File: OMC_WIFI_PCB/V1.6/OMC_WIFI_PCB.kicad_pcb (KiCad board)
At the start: 2 copper layers, 106.8 x 66.8 mm, 26 parts, among them J1 Conn_01x02_Male, J10 Conn_01x01_Male, J2 Conn_01x02_Female, J3 Conn_01x02_Male, J4 Switch, J5 Pins_FT232R, J6 Level shifter, J7 Conn_01x01_Female, J8 Regulador, J9 Conn_01x01_Female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

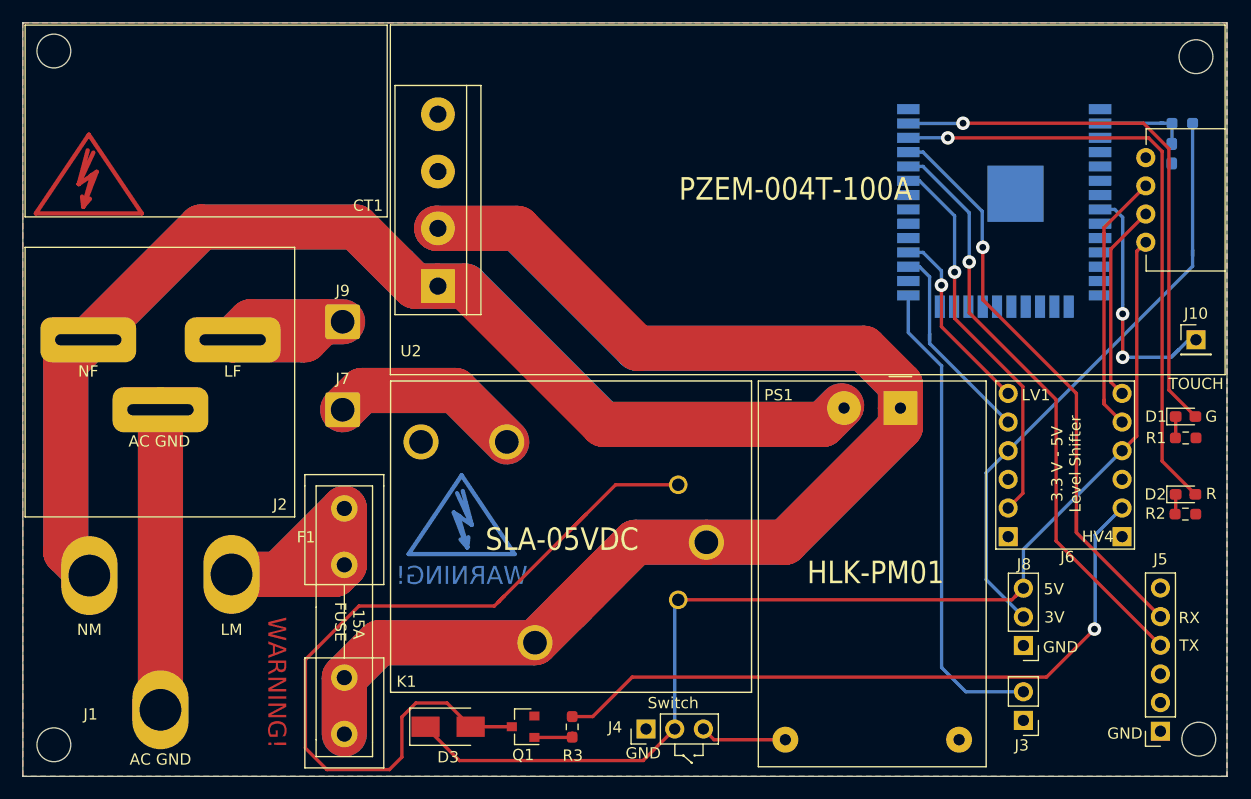
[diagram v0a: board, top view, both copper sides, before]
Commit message: Creación de versión 1.6 PCB
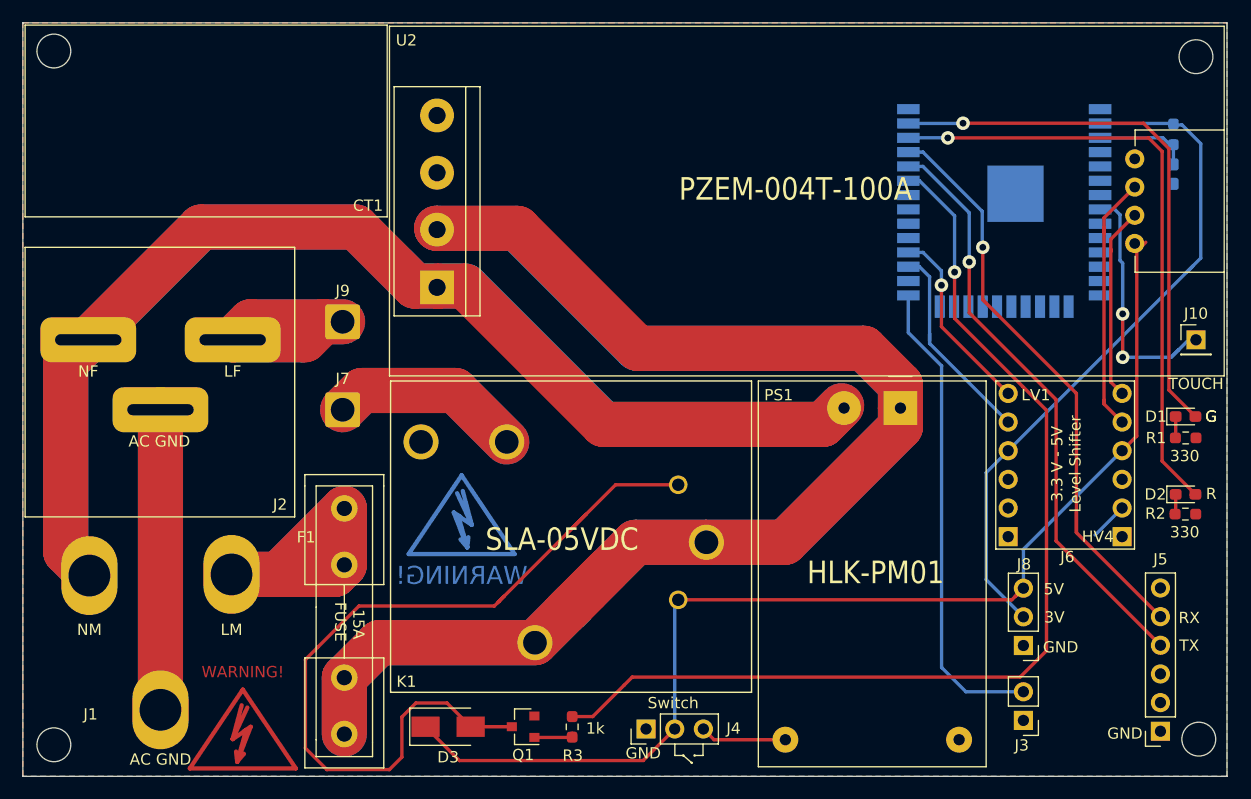
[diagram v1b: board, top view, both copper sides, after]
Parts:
- moved SYM1 51.1 mm to (595.5, -918.2)
- moved C1 1.82 mm to (678.0, -968.1)
- moved R4 1.26 mm to (678.0, -971.6), turned to 270 degrees
- moved U2 0.14 mm to (645.5, -965.7)
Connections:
- net D22_LED_G renamed D23_LED_G
- net D23_LED_R renamed D22_LED_R
- J6 pad 10: D32_RELAY_5V -> Net-(J6-Pad10)
- J6 pad 9: D32_RELAY_3V -> Net-(J6-Pad9)
- R3 pad 1: D32_RELAY_5V -> D21_RELAY
- U1 pad 2: Net-(C1-Pad1) -> +3V
- U1 pad 3: EN -> Net-(C1-Pad1)
- U1 pad 33: D32_RELAY_3V -> D21_RELAY
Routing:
- net D21_RELAY: track 0.00 -> 91.9 mm, vias 0 -> 1
- net D32_RELAY_5V: track 61.3 -> 0.00 mm, vias 1 -> 0
- net D32_RELAY_3V: track 34.3 -> 0.00 mm, vias 1 -> 0
- net +3V: track 53.2 -> 61.8 mm
- net Net-(J6-Pad10): track 0.00 -> 3.38 mm
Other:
- board text added: "10k"
- board text added: "1k"
- board text added: "1u"
- board text added: "330"
- board text added: "OMC WIFI - PCB V1.6 CG & DH 2022-07"
- board text removed: "OMC WIFI - PCB V1.5 CG & DH 2022-05"
